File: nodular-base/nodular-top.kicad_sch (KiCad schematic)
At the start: 5 parts, among them J1 Conn_01x30_MountingPin

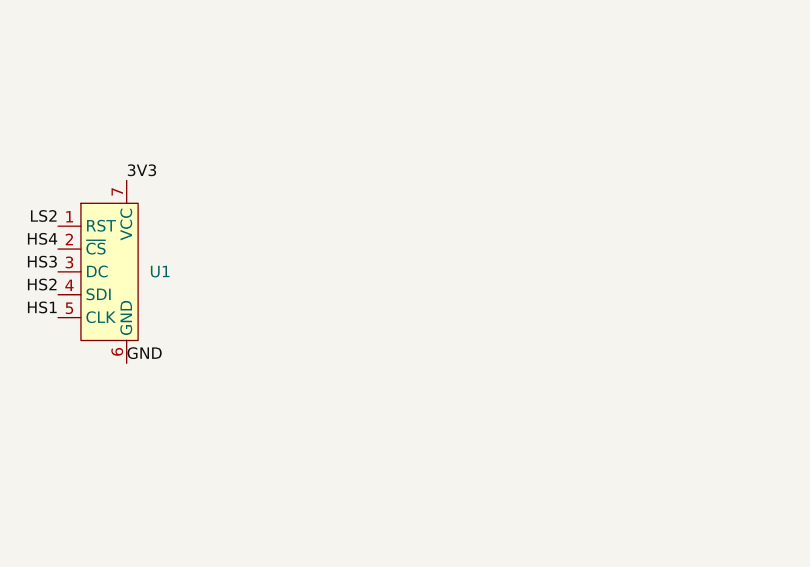
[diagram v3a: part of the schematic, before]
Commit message: Add eeprom and complete top electrical connections
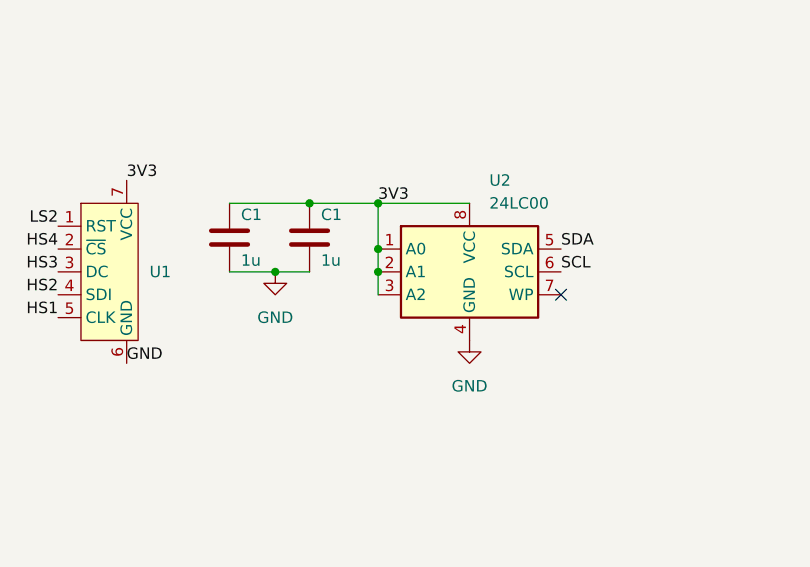
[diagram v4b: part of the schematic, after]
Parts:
- added C1 (x2): 1u, Capacitor_SMD:C_0402_1005Metric, symbol Device:C
- added U2: 24LC00, Package_SO:TSSOP-8_4.4x3mm_P0.65mm, symbol Memory_EEPROM:24LC00
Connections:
- net 3V3: now also C1.1, C1.1, U2.1 (A0), U2.2 (A1), U2.3 (A2), U2.8 (VCC)
- net GND: now also C1.2, C1.2, U2.4 (GND)
- net SCL: now also U2.6 (SCL)
- net SDA: now also U2.5 (SDA)
- no-connect marks 0 -> 1
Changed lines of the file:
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@@
 (kicad_sch (version 20230121) (generator eeschema)
   (paper "A4")
+  (junction (at 115.57 85.09) (diameter 0) (color 0 0 0 0)
+  )
+  (junction (at 115.57 82.55) (diameter 0) (color 0 0 0 0)
+  )
+  (junction (at 104.14 85.09) (diameter 0) (color 0 0 0 0)
+  )
+  (junction (at 107.95 77.47) (diameter 0) (color 0 0 0 0)
+  )
+  (junction (at 115.57 77.47) (diameter 0) (color 0 0 0 0)
+  )
+  (no_connect (at 135.89 87.63))
+  (wire (pts (xy 107.95 77.47) (xy 115.57 77.47))
+    (stroke (width 0) (type default))
+  )
   (wire (pts (xy 55.88 86.36) (xy 67.31 86.36))
     (stroke (width 0) (type default))
@@
     (stroke (width 0) (type default))
   )
+  (wire (pts (xy 104.14 85.09) (xy 107.95 85.09))
+    (stroke (width 0) (type default))
+  )
   (wire (pts (xy 195.58 77.47) (xy 185.42 77.47))
     (stroke (width 0) (type default))
   )
+  (wire (pts (xy 115.57 82.55) (xy 115.57 85.09))
+    (stroke (width 0) (type default))
+  )
   (wire (pts (xy 229.87 82.55) (xy 232.41 82.55))
     (stroke (width 0) (type default))
@@
     (stroke (width 0) (type default))
   )
+  (wire (pts (xy 125.73 77.47) (xy 115.57 77.47))
+    (stroke (width 0) (type default))
+  )
+  (wire (pts (xy 115.57 85.09) (xy 115.57 87.63))
+    (stroke (width 0) (type default))
+  )
   (wire (pts (xy 229.87 77.47) (xy 232.41 77.47))
     (stroke (width 0) (type default))
@@
     (stroke (width 0) (type default))
   )
+  (wire (pts (xy 99.06 85.09) (xy 104.14 85.09))
+    (stroke (width 0) (type default))
+  )
   (wire (pts (xy 185.42 81.28) (xy 175.26 81.28))
     (stroke (width 0) (type default))
@@
     (stroke (width 0) (type default))
   )
+  (wire (pts (xy 99.06 77.47) (xy 107.95 77.47))
+    (stroke (width 0) (type default))
+  )
   (wire (pts (xy 55.88 91.44) (xy 67.31 91.44))
+    (stroke (width 0) (type default))
+  )
+  (wire (pts (xy 115.57 77.47) (xy 115.57 82.55))
     (stroke (width 0) (type default))
   )
@@
     (effects (font (size 1.27 1.27)) (justify left bottom))
   )
+  (label "3V3" (at 115.57 77.47 0) (fields_autoplaced)
+    (effects (font (size 1.27 1.27)) (justify left bottom))
+  )
   (label "GND" (at 55.88 88.9 0) (fields_autoplaced)
     (effects (font (size 1.27 1.27)) (justify left bottom))
@@
     (effects (font (size 1.27 1.27)) (justify left bottom))
   )
+  (label "SDA" (at 135.89 82.55 0) (fields_autoplaced)
+    (effects (font (size 1.27 1.27)) (justify left bottom))
+  )
   (label "3V3" (at 55.88 93.98 0) (fields_autoplaced)
     (effects (font (size 1.27 1.27)) (justify left bottom))
@@
   )
   (label "BTN1" (at 232.41 74.93 0) (fields_autoplaced)
+    (effects (font (size 1.27 1.27)) (justify left bottom))
+  )
+  (label "SCL" (at 135.89 85.09 0) (fields_autoplaced)
     (effects (font (size 1.27 1.27)) (justify left bottom))
   )
@@
         (path "/67223bb4-fb4b-4d28-a5c8-1b64a0b88fc4"
           (reference "#FLG03") (unit 1)
+        )
+      )
+    )
+  )
+  (symbol (lib_id "Device:C") (at 107.95 81.28 0) (unit 1)
+    (in_bom yes) (on_board yes) (dnp no)
+    (property "Reference" "C1" (at 109.22 78.74 0)
+      (effects (font (size 1.27 1.27)) (justify left))
+    )
+    (property "Value" "1u" (at 109.22 83.82 0)
+      (effects (font (size 1.27 1.27)) (justify left))
+    )
+    (property "Footprint" "Capacitor_SMD:C_0402_1005Metric" (at 108.9152 85.09 0)
+      (effects (font (size 1.27 1.27)) hide)
+    )
+    (property "Datasheet" "~" (at 107.95 81.28 0)
+      (effects (font (size 1.27 1.27)) hide)
+    )
+    (pin "2")
+    (pin "1")
+    (instances
+      (project "nodular-top"
+        (path "/67223bb4-fb4b-4d28-a5c8-1b64a0b88fc4/853d8a0d-6c1f-4247-8bb7-205d5bbb87ec"
+          (reference "C1") (unit 1)
+        )
+        (path "/67223bb4-fb4b-4d28-a5c8-1b64a0b88fc4"
+          (reference "C11") (unit 1)
+        )
+      )
+    )
+  )
+  (symbol (lib_id "power:GND") (at 104.14 85.09 0) (unit 1)
+    (in_bom yes) (on_board yes) (dnp no) (fields_autoplaced)
+    (property "Reference" "#PWR07" (at 104.14 91.44 0)
+      (effects (font (size 1.27 1.27)) hide)
+    )
+    (property "Value" "GND" (at 104.14 90.17 0)
+      (effects (font (size 1.27 1.27)))
+    )
+    (property "Footprint" "" (at 104.14 85.09 0)
+      (effects (font (size 1.27 1.27)) hide)
+    )
+    (property "Datasheet" "" (at 104.14 85.09 0)
+      (effects (font (size 1.27 1.27)) hide)
+    )
+    (pin "1")
+    (instances
+      (project "nodular-top"
+        (path "/67223bb4-fb4b-4d28-a5c8-1b64a0b88fc4"
+          (reference "#PWR07") (unit 1)
         )
       )
@@
         (path "/67223bb4-fb4b-4d28-a5c8-1b64a0b88fc4"
           (reference "U1") (unit 1)
+        )
+      )
+    )
+  )
+  (symbol (lib_id "Device:C") (at 99.06 81.28 0) (unit 1)
+    (in_bom yes) (on_board yes) (dnp no)
+    (property "Reference" "C1" (at 100.33 78.74 0)
+      (effects (font (size 1.27 1.27)) (justify left))
+    )
+    (property "Value" "1u" (at 100.33 83.82 0)
+      (effects (font (size 1.27 1.27)) (justify left))
+    )
+    (property "Footprint" "Capacitor_SMD:C_0402_1005Metric" (at 100.0252 85.09 0)
+      (effects (font (size 1.27 1.27)) hide)
+    )
+    (property "Datasheet" "~" (at 99.06 81.28 0)
+      (effects (font (size 1.27 1.27)) hide)
+    )
+    (pin "2")
+    (pin "1")
+    (instances
+      (project "nodular-top"
+        (path "/67223bb4-fb4b-4d28-a5c8-1b64a0b88fc4/853d8a0d-6c1f-4247-8bb7-205d5bbb87ec"
+          (reference "C1") (unit 1)
+        )
+        (path "/67223bb4-fb4b-4d28-a5c8-1b64a0b88fc4"
+          (reference "C10") (unit 1)
         )
       )
@@
         )
       )
+    )
+  )
+  (symbol (lib_id "Memory_EEPROM:24LC00") (at 125.73 85.09 0) (unit 1)
+    (in_bom yes) (on_board yes) (dnp no) (fields_autoplaced)
+    (property "Reference" "U2" (at 127.9241 74.93 0)
+      (effects (font (size 1.27 1.27)) (justify left))
+    )
+    (property "Value" "24LC00" (at 127.9241 77.47 0)
+      (effects (font (size 1.27 1.27)) (justify left))
+    )
+    (property "Footprint" "Package_SO:TSSOP-8_4.4x3mm_P0.65mm" (at 125.73 85.09 0)
+      (effects (font (size 1.27 1.27)) hide)
+    )
+    (property "Datasheet" "http://ww1.microchip.com/downloads/en/DeviceDoc/21178G.pdf" (at 125.73 85.09 0)
+      (effects (font (size 1.27 1.27)) hide)
+    )
+    (pin "2")
+    (pin "3")
+    (pin "6")
+    (pin "7")
+    (pin "1")
+    (pin "4")
+    (pin "8")
+    (pin "5")
+    (instances
+      (project "nodular-top"
+        (path "/67223bb4-fb4b-4d28-a5c8-1b64a0b88fc4"
+          (reference "U2") (unit 1)
+        )
+      )
+    )
+  )
+  (symbol (lib_id "power:GND") (at 125.73 92.71 0) (unit 1)
+    (in_bom yes) (on_board yes) (dnp no) (fields_autoplaced)
+    (property "Reference" "#PWR06" (at 125.73 99.06 0)
+      (effects (font (size 1.27 1.27)) hide)
+    )
+    (property "Value" "GND" (at 125.73 97.79 0)
+      (effects (font (size 1.27 1.27)))
+    )
+    (property "Footprint" "" (at 125.73 92.71 0)
+      (effects (font (size 1.27 1.27)) hide)
+    )
+    (property "Datasheet" "" (at 125.73 92.71 0)
+      (effects (font (size 1.27 1.27)) hide)
+    )
+    (pin "1")
+    (instances
+      (project "nodular-top"
+        (path "/67223bb4-fb4b-4d28-a5c8-1b64a0b88fc4"
+          (reference "#PWR06") (unit 1)
+        )
+      )

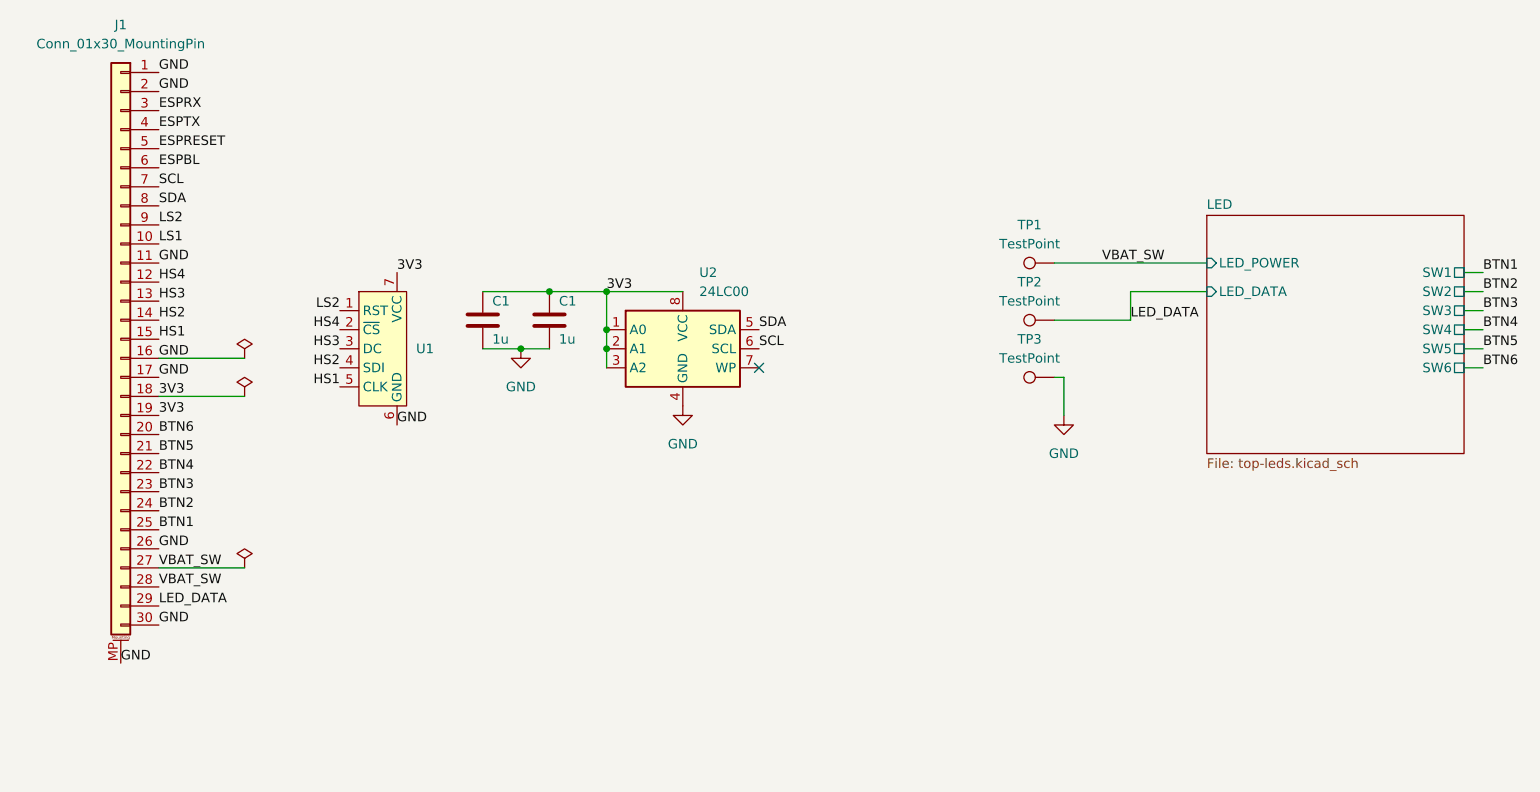
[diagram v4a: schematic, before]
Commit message: Update top board layout, rename libraries
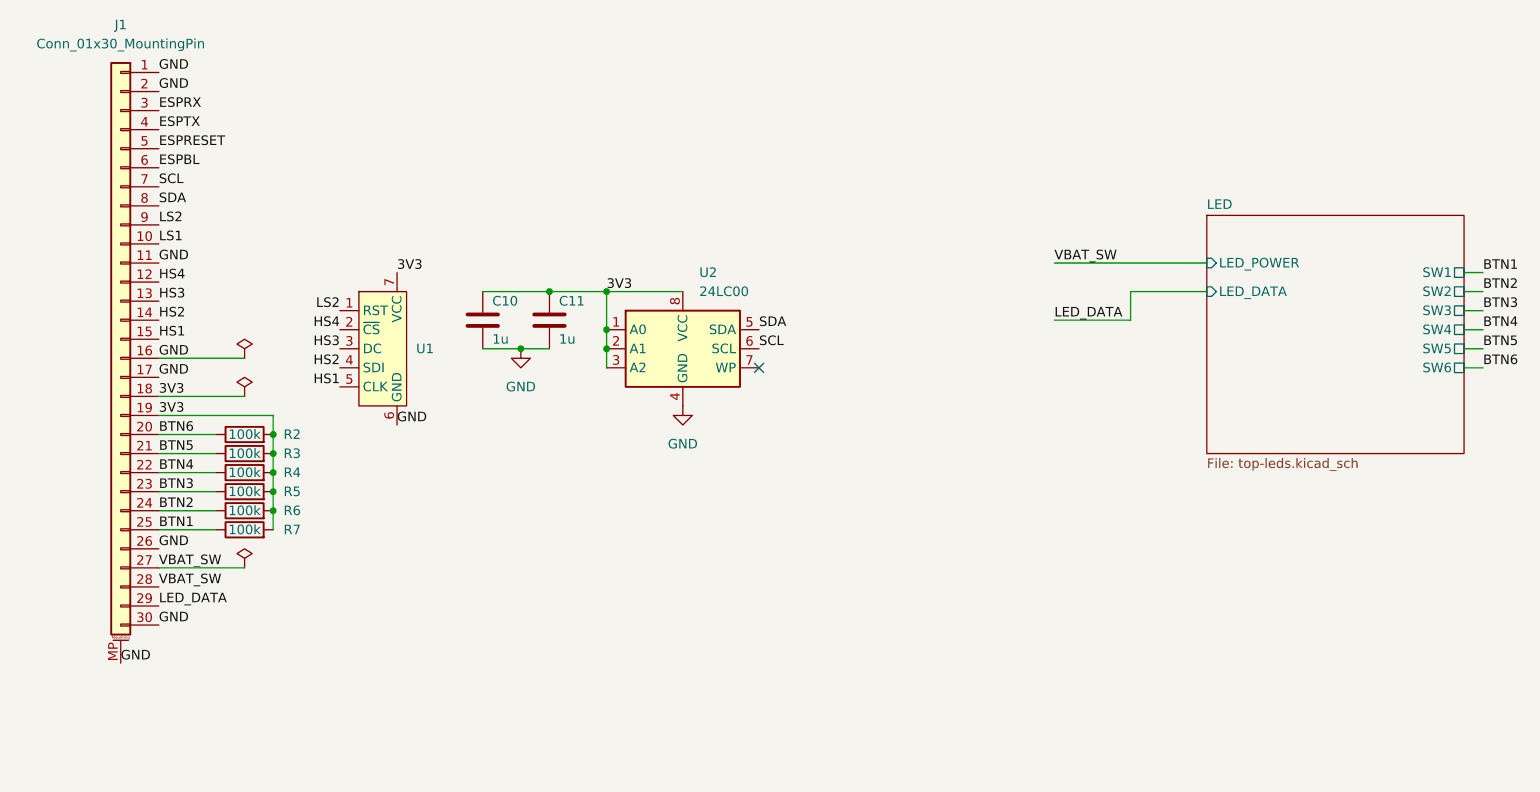
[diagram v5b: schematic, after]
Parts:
- removed TP1, TP2, TP3: TestPoint, TestPoint:TestPoint_Pad_4.0x4.0mm, symbol Connector:TestPoint
- added R2, R3, R4, R5, R6, R7: 100k, Resistor_SMD:R_0402_1005Metric, symbol Device:R
- renumbered C1 to C10, C1 to C11
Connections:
- net 3V3: now also R2.2, R3.2, R4.2, R5.2, R6.2, R7.2
- net BTN1: now also R7.1
- net BTN2: now also R6.1
- net BTN3: now also R5.1
- net BTN4: now also R4.1
- net BTN5: now also R3.1
- net BTN6: now also R2.1
